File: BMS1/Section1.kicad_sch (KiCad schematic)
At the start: 68 parts

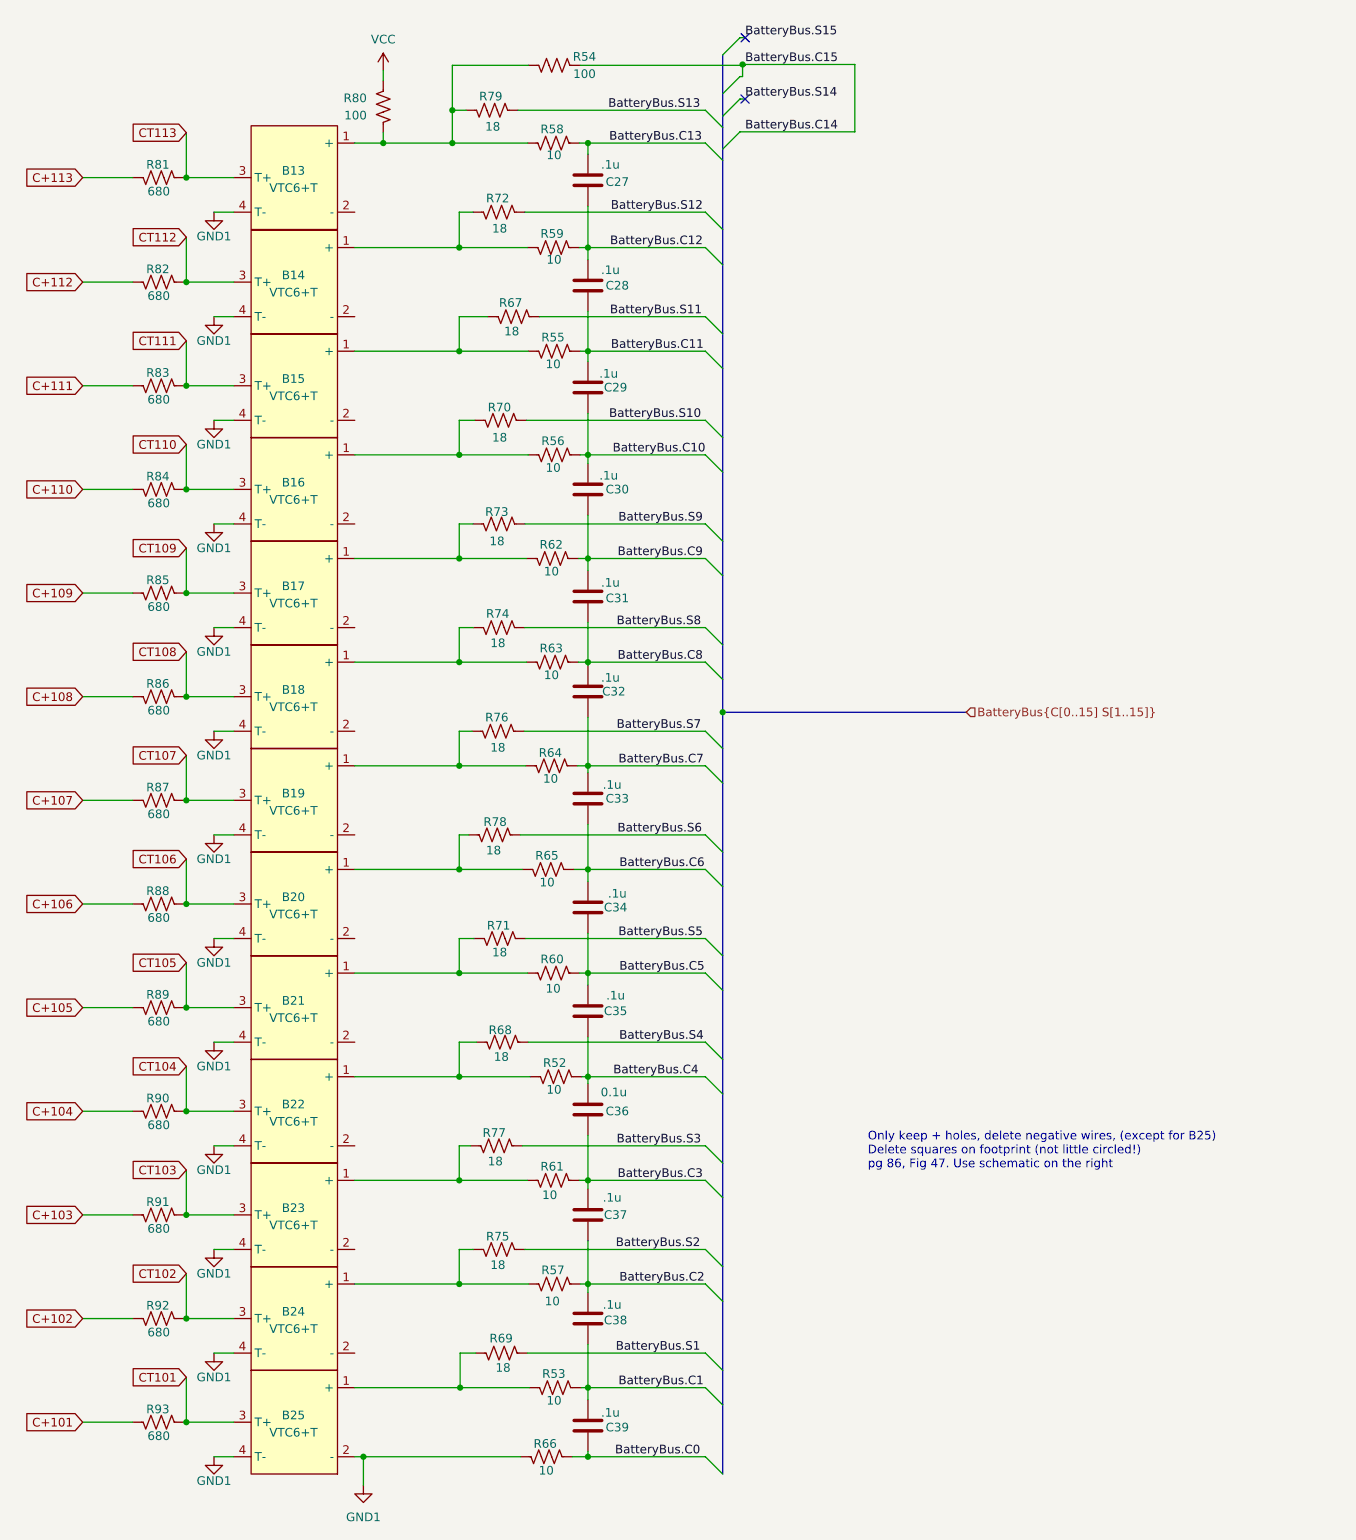
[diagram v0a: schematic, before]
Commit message: ERC fixes
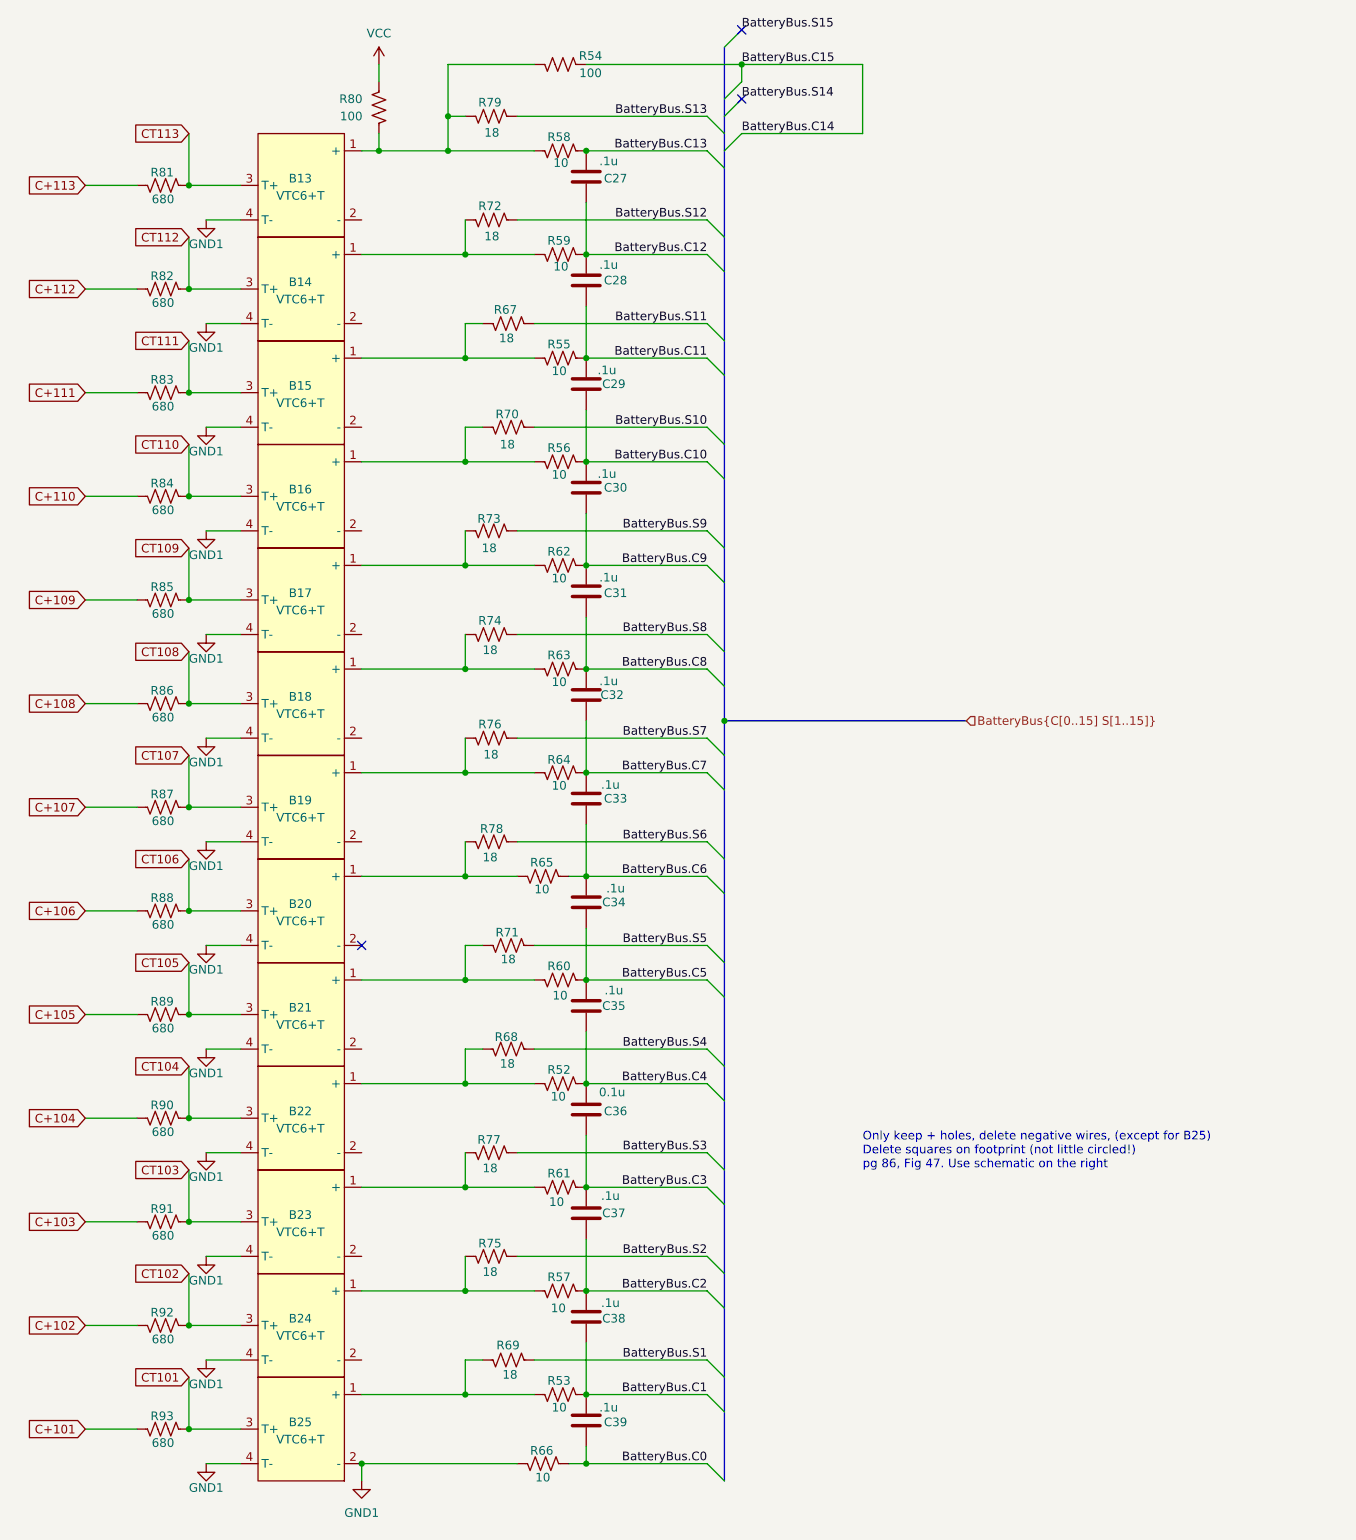
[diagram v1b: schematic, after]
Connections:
- no-connect marks 2 -> 3
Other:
- moved on the sheet: B13, B14, B15, B16, B17, B18, B19, B20, B21, B22, B23, B24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

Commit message: ERC error fixes
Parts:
- removed B13, B14, B15, B16, B17, B18, B19, B20, B21, B22, B23, B24: VTC6+T, AERO_Footprints:VTC-6, symbol AERO_Symbols:VTC6+T
- added B13, B14, B15, B16, B17, B18, B19, B20, B21, B22, B23, B24: VTC6+T-single, AERO_Footprints:VTC-6-single, symbol AERO:VTC6+T-single
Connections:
- net CT102: now also B24.3 (T+)
- net CT103: now also B23.3 (T+)
- net CT104: now also B22.3 (T+)
- net CT105: now also B21.3 (T+)
- net CT106: now also B20.3 (T+)
- net CT107: now also B19.3 (T+)
- net CT108: now also B18.3 (T+)
- net CT109: now also B17.3 (T+)
- net CT110: now also B16.3 (T+)
- net CT111: now also B15.3 (T+)
- net CT112: now also B14.3 (T+)
- net CT113: now also B13.3 (T+)
- net GND1: now also B13.2 (T-), B14.2 (T-), B15.2 (T-), B16.2 (T-), B17.2 (T-), B18.2 (T-), B19.2 (T-), B20.2 (T-), B21.2 (T-), B22.2 (T-), B23.2 (T-), B24.2 (T-)
- net at R61.1, R77.1: now also B23.1 (+)
- net at R63.1, R74.1: now also B18.1 (+)
- net at R52.1, R68.1: now also B22.1 (+)
- net at R64.1, R76.1: now also B19.1 (+)
- net at R54.2, R58.1, R79.1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: now also B13.1 (+)
- net at R62.1, R73.1: now also B17.1 (+)
- net at R60.1, R71.1: now also B21.1 (+)
- net at R56.1, R70.1: now also B16.1 (+)
- net at R59.1, R72.1: now also B14.1 (+)
- net at R57.1, R75.1: now also B24.1 (+)
- net at R65.1, R78.1: now also B20.1 (+)
- net at R55.1, R67.1: now also B15.1 (+)
- no-connect marks 3 -> 2
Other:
- note removed: "Only keep + holes, delete negative wires, (except for B25) Delete squares on footprint (not little circled!) pg 86, Fig 47. Use schematic on the right"

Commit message: Footprints
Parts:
- C27, C28, C29, C30, C31, C32, C33, C34, C35, C37, C38, C39: value .1u -> 0.1uF; footprint Capacitor_SMD:C_0603_1608Metric_Pad1.08x0.95mm_HandSolder -> Capacitor_SMD:C_0603_1608Metric; MPN (none) -> AGC0603X7R101-104KXP
- C36: value 0.1u -> 0.1uF; footprint Capacitor_SMD:C_0603_1608Metric_Pad1.08x0.95mm_HandSolder -> Capacitor_SMD:C_0603_1608Metric; MPN (none) -> AGC0603X7R101-104KXP
- R52, R53, R55, R56, R57, R58, R59, R60, R61, R62, R63, R64, R65, R66: footprint Resistor_SMD:R_0805_2012Metric_Pad1.20x1.40mm_HandSolder -> Resistor_SMD:R_0805_2012Metric
- R54: footprint Resistor_SMD:R_0603_1608Metric_Pad0.98x0.95mm_HandSolder -> Resistor_SMD:R_0805_2012Metric
- R67, R68, R69, R70, R71, R72, R73, R74, R75, R76, R77, R78: footprint Resistor_SMD:R_2512_6332Metric_Pad1.40x3.35mm_HandSolder -> Resistor_SMD:R_2512_6332Metric
- R79, R80, R81, R82, R83, R84, R85, R86, R87, R88, R89, R90, R91, R92, R93: footprint Resistor_SMD:R_0603_1608Metric_Pad0.98x0.95mm_HandSolder -> Resistor_SMD:R_0603_1608Metric

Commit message: Footprints
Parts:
- R52, R53, R55, R56, R57, R58, R59, R60, R61, R62, R63, R64, R65, R66: MPN (none) -> ERJ-P06J100V
- R54: MPN (none) -> RMCF0805FT100R
- R80: MPN (none) -> ERJ-3EKF1000V
- R81, R82, R83, R84, R85, R86, R87, R88, R89, R90, R91, R92, R93: MPN (none) -> RC0603JR-07680RL
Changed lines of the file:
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@@
 			)
 		)
-		(property "Datasheet" "~"
+		(property "Datasheet" "https://industrial.panasonic.com/cdbs/www-data/pdf/RDO0000/AOA0000C331.pdf"
 			(at 95.25 187.96 0)
 			(effects
@@
 			)
 		)
-		(property "MPN" ""
+		(property "MPN" "ERJ-P06J100V"
 			(at 95.25 187.96 0)
 			(effects
@@
 			)
 		)
-		(property "Datasheet" "~"
+		(property "Datasheet" "https://www.seielect.com/catalog/sei-rmcf_rmcp.pdf"
 			(at 95.25 22.86 0)
 			(effects
@@
 			)
 		)
-		(property "MPN" ""
+		(property "MPN" "RMCF0805FT100R"
 			(at 95.25 22.86 0)
 			(effects
@@
 			)
 		)
-		(property "Datasheet" "~"
+		(property "Datasheet" "https://industrial.panasonic.com/cdbs/www-data/pdf/RDO0000/AOA0000C331.pdf"
 			(at 95.25 96.52 0)
 			(effects
@@
 			)
 		)
-		(property "MPN" ""
+		(property "MPN" "ERJ-P06J100V"
 			(at 95.25 96.52 0)
 			(effects
@@
 			)
 		)
-		(property "Datasheet" "~"
+		(property "Datasheet" "https://industrial.panasonic.com/cdbs/www-data/pdf/RDO0000/AOA0000C331.pdf"
 			(at 92.71 228.6 0)
 			(effects
@@
 			)
 		)
-		(property "MPN" ""
+		(property "MPN" "ERJ-P06J100V"
 			(at 92.71 228.6 0)
 			(effects
@@
 			)
 		)
-		(property "Datasheet" "~"
+		(property "Datasheet" "https://www.yageo.com/upload/media/product/products/datasheet/rchip/PYu-RC_Group_51_RoHS_L_12.pdf"
 			(at 36.83 162.56 0)
 			(effects
@@
 			)
 		)
-		(property "MPN" ""
+		(property "MPN" "RC0603JR-07680RL"
 			(at 36.83 162.56 0)
 			(effects
@@
 			)
 		)
-		(property "Datasheet" "~"
+		(property "Datasheet" "https://www.yageo.com/upload/media/product/products/datasheet/rchip/PYu-RC_Group_51_RoHS_L_12.pdf"
 			(at 36.83 71.12 0)
 			(effects
@@
 			)
 		)
-		(property "MPN" ""
+		(property "MPN" "RC0603JR-07680RL"
 			(at 36.83 71.12 0)
 			(effects
@@
 			)
 		)
-		(property "Datasheet" "~"
+		(property "Datasheet" "https://industrial.panasonic.com/cdbs/www-data/pdf/RDO0000/AOA0000C331.pdf"
 			(at 95.25 218.44 0)
 			(effects
@@
 			)
 		)
-		(property "MPN" ""
+		(property "MPN" "ERJ-P06J100V"
 			(at 95.25 218.44 0)
 			(effects
@@
 			)
 		)
-		(property "Datasheet" "~"
+		(property "Datasheet" "https://industrial.panasonic.com/cdbs/www-data/pdf/RDO0000/AOA0000C331.pdf"
 			(at 95.25 81.28 0)
 			(effects
@@
 			)
 		)
-		(property "MPN" ""
+		(property "MPN" "ERJ-P06J100V"
 			(at 95.25 81.28 0)
 			(effects
@@
 			)
 		)
-		(property "Datasheet" "~"
+		(property "Datasheet" "https://industrial.panasonic.com/cdbs/www-data/pdf/RDO0000/AOA0000C331.pdf"
 			(at 95.25 127 0)
 			(effects
@@
 			)
 		)
-		(property "MPN" ""
+		(property "MPN" "ERJ-P06J100V"
 			(at 95.25 127 0)
 			(effects
@@
 			)
 		)
-		(property "Datasheet" "~"
+		(property "Datasheet" "https://www.yageo.com/upload/media/product/products/datasheet/rchip/PYu-RC_Group_51_RoHS_L_12.pdf"
 			(at 36.83 86.36 0)
 			(effects
@@
 			)
 		)
-		(property "MPN" ""
+		(property "MPN" "RC0603JR-07680RL"
 			(at 36.83 86.36 0)
 			(effects
@@
 			)
 		)
-		(property "Datasheet" "~"
+		(property "Datasheet" "https://www.yageo.com/upload/media/product/products/datasheet/rchip/PYu-RC_Group_51_RoHS_L_12.pdf"
 			(at 36.83 193.04 0)
 			(effects
@@
 			)
 		)
-		(property "MPN" ""
+		(property "MPN" "RC0603JR-07680RL"
 			(at 36.83 193.04 0)
 			(effects
@@
 			)
 		)
-		(property "Datasheet" "~"
+		(property "Datasheet" "https://industrial.panasonic.com/cdbs/www-data/pdf/RDO0000/AOA0000C331.pdf"
 			(at 95.25 50.8 0)
 			(effects
@@
 			)
 		)
-		(property "MPN" ""
+		(property "MPN" "ERJ-P06J100V"
 			(at 95.25 50.8 0)
 			(effects
@@
 			)
 		)
-		(property "Datasheet" "~"
+		(property "Datasheet" "https://industrial.panasonic.com/cdbs/www-data/pdf/RDO0000/AOA0000C331.pdf"
 			(at 95.25 157.48 0)
 			(effects
@@
 			)
 		)
-		(property "MPN" ""
+		(property "MPN" "ERJ-P06J100V"
 			(at 95.25 157.48 0)
 			(effects
@@
 			)
 		)
-		(property "Datasheet" "~"
+		(property "Datasheet" "https://www.yageo.com/upload/media/product/products/datasheet/rchip/PYu-RC_Group_51_RoHS_L_12.pdf"
 			(at 36.83 40.64 0)
 			(effects
@@
 			)
 		)
-		(property "MPN" ""
+		(property "MPN" "RC0603JR-07680RL"
 			(at 36.83 40.64 0)
 			(effects
@@
 			)
 		)
-		(property "Datasheet" "~"
+		(property "Datasheet" "https://www.yageo.com/upload/media/product/products/datasheet/rchip/PYu-RC_Group_51_RoHS_L_12.pdf"
 			(at 36.83 132.08 0)
 			(effects
@@
 			)
 		)
-		(property "MPN" ""
+		(property "MPN" "RC0603JR-07680RL"
 			(at 36.83 132.08 0)
 			(effects
@@
 			)
 		)
-		(property "Datasheet" "~"
+		(property "Datasheet" "https://industrial.panasonic.com/cdbs/www-data/pdf/RDO0000/AOA0000C331.pdf"
 			(at 92.71 142.24 0)
 			(effects
@@
 			)
 		)
-		(property "MPN" ""
+		(property "MPN" "ERJ-P06J100V"
 			(at 92.71 142.24 0)
 			(effects
@@
 			)
 		)
-		(property "Datasheet" "~"
+		(property "Datasheet" "https://www.yageo.com/upload/media/product/products/datasheet/rchip/PYu-RC_Group_51_RoHS_L_12.pdf"
 			(at 36.83 116.84 0)
 			(effects
@@
 			)
 		)
-		(property "MPN" ""
+		(property "MPN" "RC0603JR-07680RL"
 			(at 36.83 116.84 0)
 			(effects
@@
 			)
 		)
-		(property "Datasheet" "~"
+		(property "Datasheet" "https://www.yageo.com/upload/media/product/products/datasheet/rchip/PYu-RC_Group_51_RoHS_L_12.pdf"
 			(at 36.83 223.52 0)
 			(effects
@@
 			)
 		)
-		(property "MPN" ""
+		(property "MPN" "RC0603JR-07680RL"
 			(at 36.83 223.52 0)
 			(effects
@@
 			)
 		)
-		(property "Datasheet" "~"
+		(property "Datasheet" "https://industrial.panasonic.com/cdbs/www-data/pdf/RDO0000/AOA0000C331.pdf"
 			(at 95.25 172.72 0)
 			(effects
@@
 			)
 		)
-		(property "MPN" ""
+		(property "MPN" "ERJ-P06J100V"
 			(at 95.25 172.72 0)
 			(effects
@@
 			)
 		)
-		(property "Datasheet" "~"
+		(property "Datasheet" "https://industrial.panasonic.com/cdbs/www-data/pdf/RDO0000/AOA0000C331.pdf"
 			(at 95.25 35.56 0)
 			(effects
@@
 			)
 		)
-		(property "MPN" ""
+		(property "MPN" "ERJ-P06J100V"
 			(at 95.25 35.56 0)
 			(effects
@@
 			)
 		)
-		(property "Datasheet" "~"
+		(property "Datasheet" "https://www.yageo.com/upload/media/product/products/datasheet/rchip/PYu-RC_Group_51_RoHS_L_12.pdf"
 			(at 36.83 147.32 0)
 			(effects
@@
 			)
 		)
-		(property "MPN" ""
+		(property "MPN" "RC0603JR-07680RL"
 			(at 36.83 147.32 0)
 			(effects
@@
 			)
 		)
-		(property "Datasheet" "~"
+		(property "Datasheet" "https://www.yageo.com/upload/media/product/products/datasheet/rchip/PYu-RC_Group_51_RoHS_L_12.pdf"
 			(at 36.83 101.6 0)
 			(effects
@@
 			)
 		)
-		(property "MPN" ""
+		(property "MPN" "RC0603JR-07680RL"
 			(at 36.83 101.6 0)
 			(effects
@@
 			)
 		)
-		(property "Datasheet" "~"
+		(property "Datasheet" "https://www.yageo.com/upload/media/product/products/datasheet/rchip/PYu-RC_Group_51_RoHS_L_12.pdf"
 			(at 36.83 55.88 0)
 			(effects
@@
 			)
 		)
-		(property "MPN" ""
+		(property "MPN" "RC0603JR-07680RL"
 			(at 36.83 55.88 0)
 			(effects
@@
 			)
 		)
-		(property "Datasheet" "~"
+		(property "Datasheet" "https://www.yageo.com/upload/media/product/products/datasheet/rchip/PYu-RC_Group_51_RoHS_L_12.pdf"
 			(at 36.83 208.28 0)
 			(effects
@@
 			)
 		)
-		(property "MPN" ""
+		(property "MPN" "RC0603JR-07680RL"
 			(at 36.83 208.28 0)
 			(effects
@@
 			)
 		)
-		(property "Datasheet" "~"
+		(property "Datasheet" "https://industrial.panasonic.com/cdbs/www-data/pdf/RDA0000/AOA0000C304.pdf"
 			(at 68.58 29.21 0)
 			(effects
@@
 			)
 		)
-		(property "MPN" ""
+		(property "MPN" "ERJ-3EKF1000V"
 			(at 68.58 29.21 0)
 			(effects
@@
 			)
 		)
-		(property "Datasheet" "~"
+		(property "Datasheet" "https://industrial.panasonic.com/cdbs/www-data/pdf/RDO0000/AOA0000C331.pdf"
 			(at 95.25 111.76 0)
 			(effects
@@
 			)
 		)
-		(property "MPN" ""
+		(property "MPN" "ERJ-P06J100V"
 			(at 95.25 111.76 0)
 			(effects
@@
 			)
 		)
-		(property "Datasheet" "~"
+		(property "Datasheet" "https://industrial.panasonic.com/cdbs/www-data/pdf/RDO0000/AOA0000C331.pdf"
 			(at 95.25 66.04 0)
 			(effects
@@
 			)
 		)
-		(property "MPN" ""
+		(property "MPN" "ERJ-P06J100V"
 			(at 95.25 66.04 0)
 			(effects
@@
 			)
 		)
-		(property "Datasheet" "~"
+		(property "Datasheet" "https://www.yageo.com/upload/media/product/products/datasheet/rchip/PYu-RC_Group_51_RoHS_L_12.pdf"
 			(at 36.83 177.8 0)
 			(effects
@@
 			)
 		)
-		(property "MPN" ""
+		(property "MPN" "RC0603JR-07680RL"
 			(at 36.83 177.8 0)
 			(effects
@@
 			)
 		)
-		(property "Datasheet" "~"
+		(property "Datasheet" "https://industrial.panasonic.com/cdbs/www-data/pdf/RDO0000/AOA0000C331.pdf"
 			(at 95.25 203.2 0)
 			(effects
@@
 			)
 		)
-		(property "MPN" ""
+		(property "MPN" "ERJ-P06J100V"
 			(at 95.25 203.2 0)
 			(effects
